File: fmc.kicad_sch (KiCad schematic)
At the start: 2 parts, among them P1 ASP-134604-01, P2 ASP-134604-01

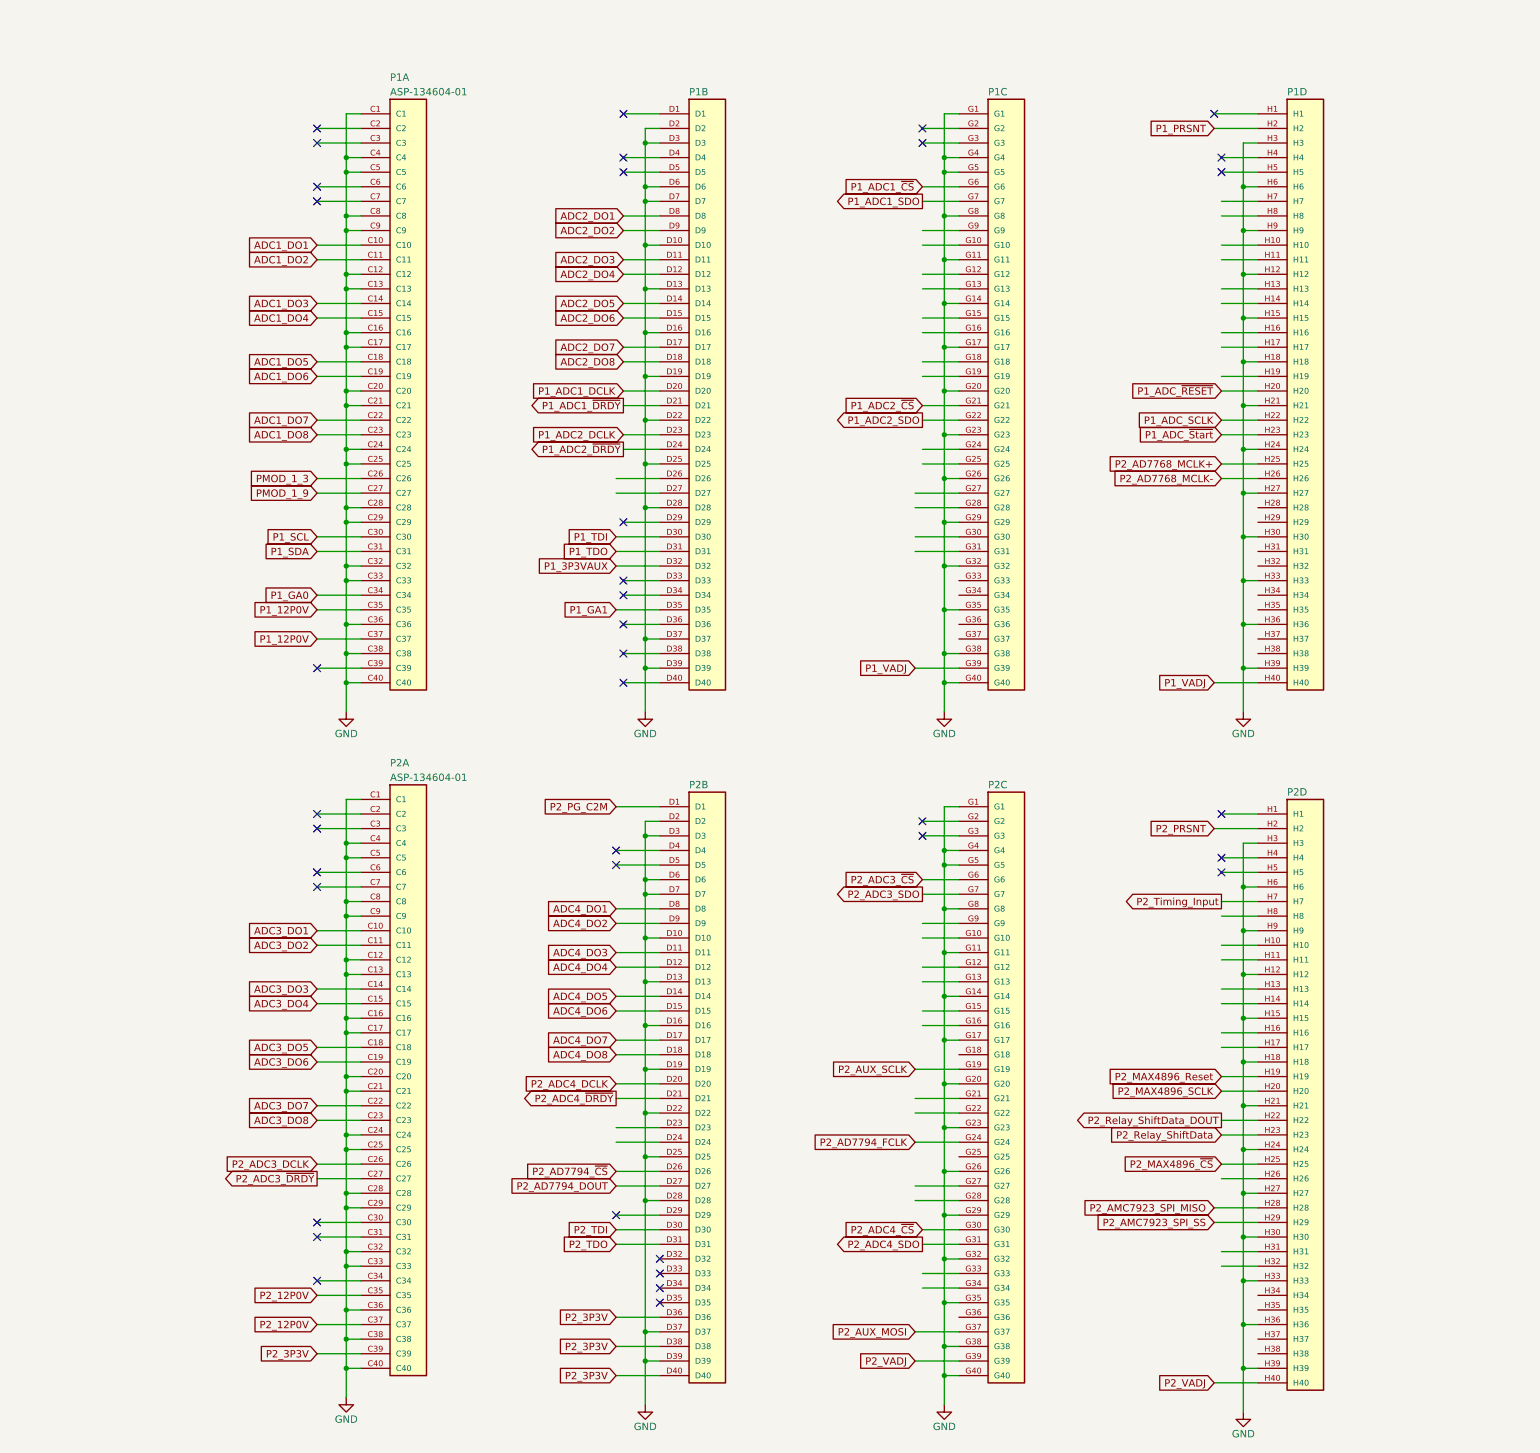
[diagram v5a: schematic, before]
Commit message: Updated Schematics
Changes:
-Moved Input resistors to after Coupling Relay
-Added diff cap at ADC input
-Changed the ADC clocking configuration (added quad LVDS driver)
-Changed some signal names for consistancy
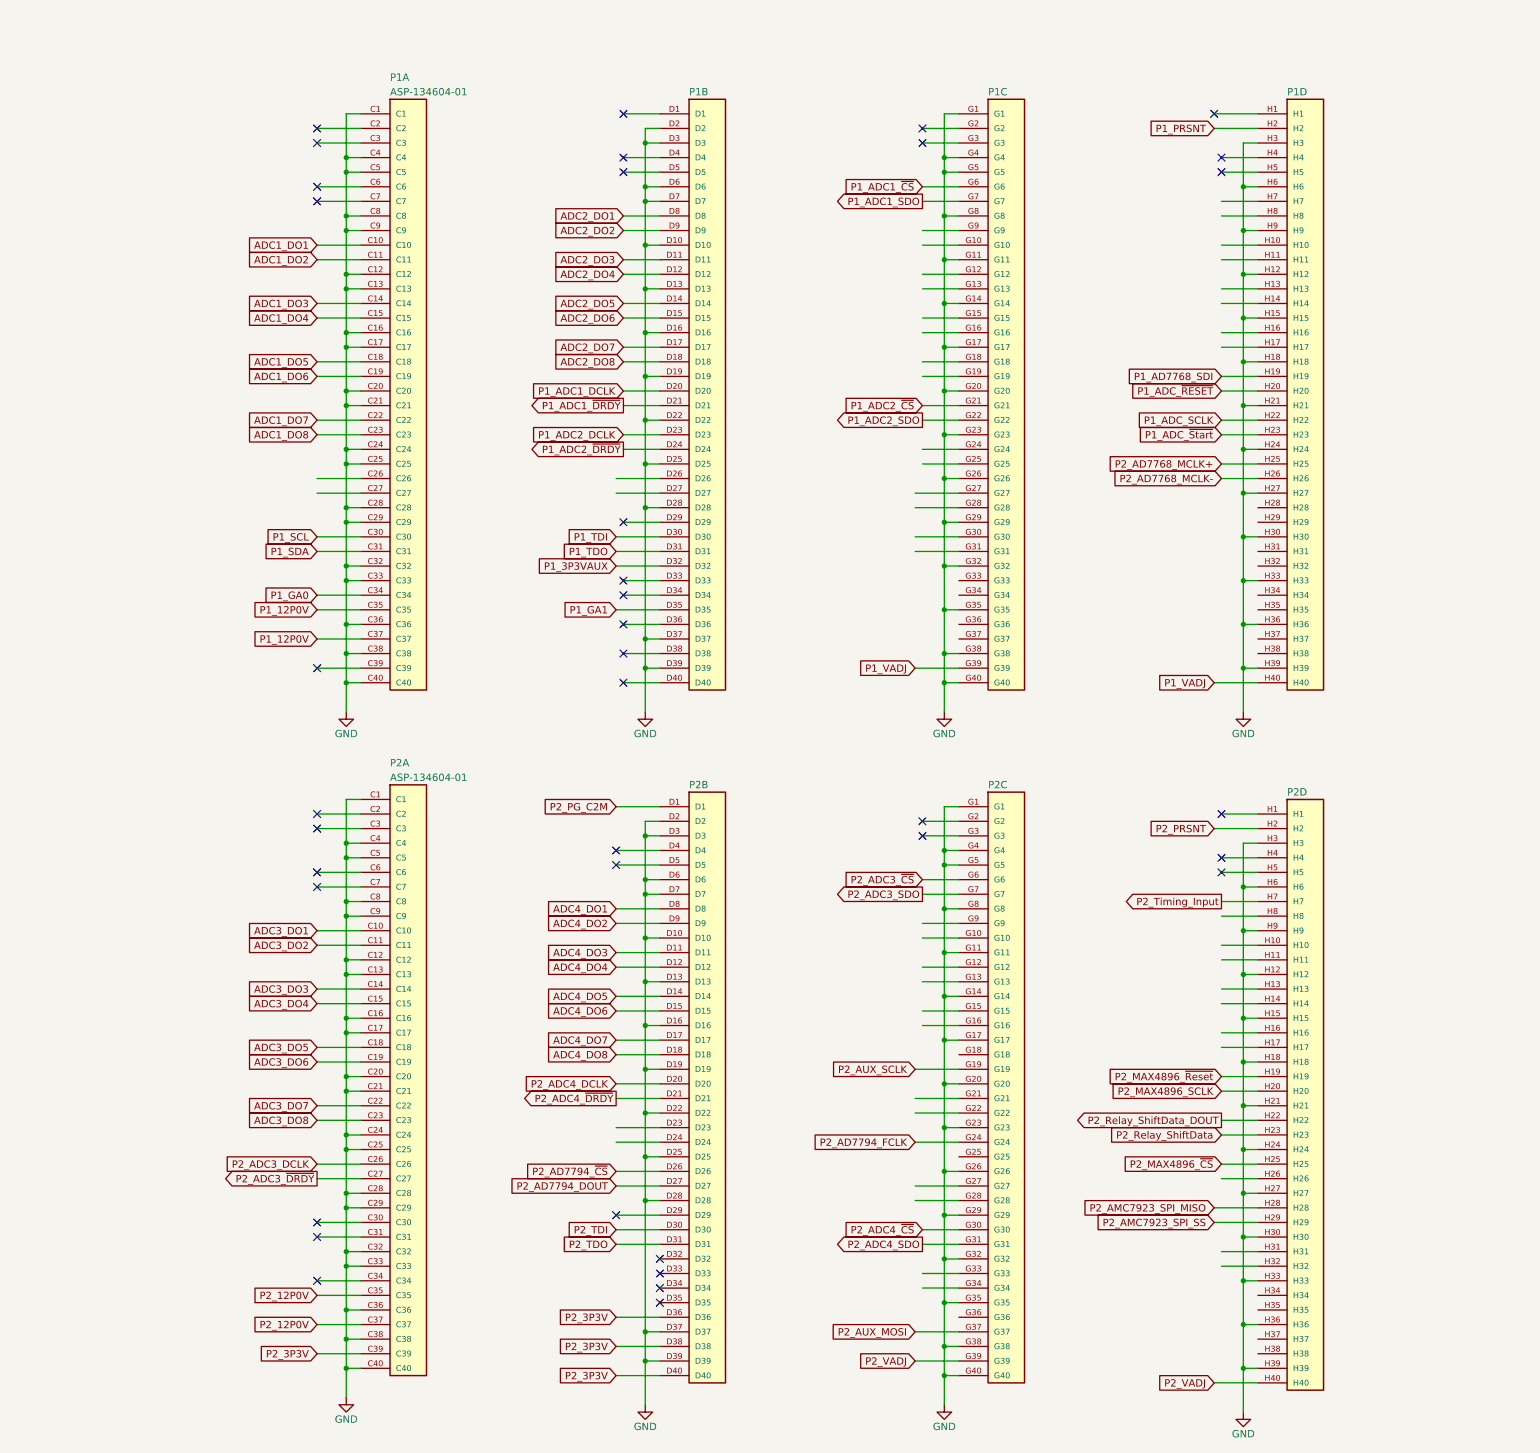
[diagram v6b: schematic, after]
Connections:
- net P1_AD7768_SDI: now reaches P1.H19
- net P2_MAX4896_Reset renamed P2_MAX4896_~{Reset}
- net PMOD_1_3: no longer names the net of P1.C26
- net PMOD_1_9: no longer names the net of P1.C27
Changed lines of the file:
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@@
-    )
-  )
-  (global_label "PMOD_1_9" (shape input) (at 118.11 97.79 180) (fields_autoplaced)
-    (effects (font (size 1.27 1.27)) (justify right))
-    (property "Intersheetrefs" "${INTERSHEET_REFS}" (at 105.5281 97.79 0)
-      (effects (font (size 1.27 1.27)) (justify right) hide)
     )
   )
@@
     )
   )
-  (global_label "P2_MAX4896_Reset" (shape input) (at 275.59 199.39 180) (fields_autoplaced)
+  (global_label "P2_MAX4896_~{Reset}" (shape input) (at 275.59 199.39 180) (fields_autoplaced)
     (effects (font (size 1.27 1.27)) (justify right))
     (property "Intersheetrefs" "${INTERSHEET_REFS}" (at 254.4016 199.39 0)
@@
     )
   )
-  (global_label "PMOD_1_3" (shape input) (at 118.11 95.25 180) (fields_autoplaced)
-    (effects (font (size 1.27 1.27)) (justify right))
-    (property "Intersheetrefs" "${INTERSHEET_REFS}" (at 105.5281 95.25 0)
-      (effects (font (size 1.27 1.27)) (justify right) hide)
-    )
-  )
   (global_label "ADC2_DO7" (shape input) (at 171.45 72.39 180) (fields_autoplaced)
     (effects (font (size 1.27 1.27)) (justify right))
@@
       (effects (font (size 1.27 1.27)) (justify right) hide)
     )
+  )
+  (global_label "P1_AD7768_SDI" (shape input) (at 275.59 77.47 180) (fields_autoplaced)
+    (effects (font (size 1.27 1.27)) (justify right))
+    (property "Intersheetrefs" "${INTERSHEET_REFS}" (at 257.9092 77.47 0)
+      (effects (font (size 1.27 1.27)) (justify right) hide)
+    )

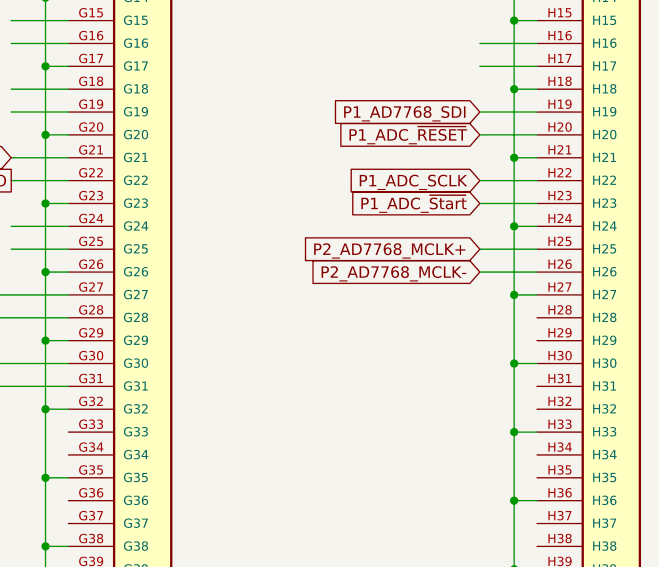
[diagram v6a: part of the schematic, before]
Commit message: Updated Schematics with latest suggestions
updates:
-Revised Power supply section
-Changed clock buffer chip for ADC Clock
- Added additional no pop & jumper parts for board debugging
-Other small part changes
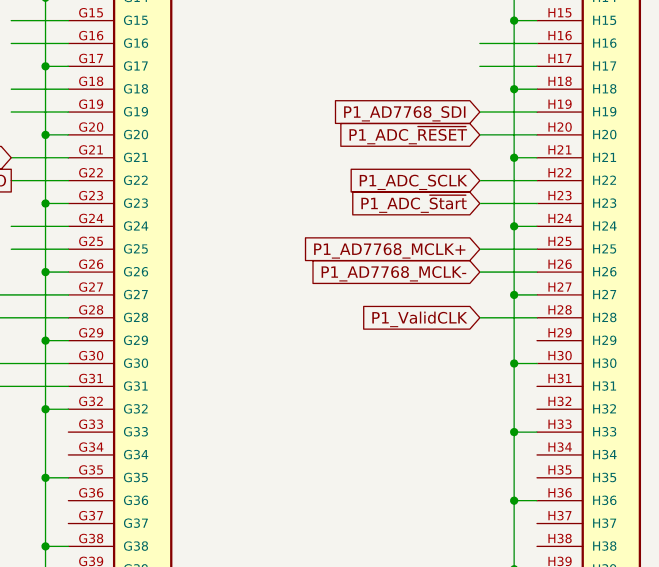
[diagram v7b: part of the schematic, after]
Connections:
- net P1_ValidCLK: now reaches P1.H28
- net P2_AD7768_MCLK+ renamed P1_AD7768_MCLK+
- net P2_AD7768_MCLK- renamed P1_AD7768_MCLK-
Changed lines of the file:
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@@
+    (stroke (width 0) (type default))
+  )
+  (wire (pts (xy 275.59 100.33) (xy 281.94 100.33))
     (stroke (width 0) (type default))
   )
@@
     )
   )
-  (global_label "P2_AD7768_MCLK-" (shape input) (at 275.59 95.25 180) (fields_autoplaced)
+  (global_label "P1_AD7768_MCLK-" (shape input) (at 275.59 95.25 180) (fields_autoplaced)
     (effects (font (size 1.27 1.27)) (justify right))
     (property "Intersheetrefs" "${INTERSHEET_REFS}" (at 254.4016 95.25 0)
@@
     )
   )
+  (global_label "P1_ValidCLK" (shape input) (at 275.59 100.33 180) (fields_autoplaced)
+    (effects (font (size 1.27 1.27)) (justify right))
+    (property "Intersheetrefs" "${INTERSHEET_REFS}" (at 260.933 100.33 0)
+      (effects (font (size 1.27 1.27)) (justify right) hide)
+    )
+  )
   (global_label "P2_TDI" (shape input) (at 170.18 226.06 180) (fields_autoplaced)
     (effects (font (size 1.27 1.27)) (justify right))
@@
     )
   )
-  (global_label "P2_AD7768_MCLK+" (shape input) (at 275.59 92.71 180) (fields_autoplaced)
+  (global_label "P1_AD7768_MCLK+" (shape input) (at 275.59 92.71 180) (fields_autoplaced)
     (effects (font (size 1.27 1.27)) (justify right))
     (property "Intersheetrefs" "${INTERSHEET_REFS}" (at 254.4016 92.71 0)
